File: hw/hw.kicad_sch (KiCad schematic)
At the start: 94 parts, among them U4 TPM8205ATS6

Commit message: wip
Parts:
- gave numbers to parts that had none: 89
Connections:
- net PWM1: now also U1.31 (GPIO20); no longer U1.8 (GPIO6)
- net PWM2: now also U1.32 (GPIO21); no longer U1.9 (GPIO7)
- net PWM3: now also U1.27 (GPIO16); no longer U1.11 (GPIO8)
- net PWM4: now also U1.29 (GPIO18); no longer U1.12 (GPIO9)
- net PWM5: now also U1.15 (GPIO12); no longer U1.13 (GPIO10)
- net PWM6: now also U1.17 (GPIO14); no longer U1.14 (GPIO11)
- net PWM7: now also U1.11 (GPIO8); no longer U1.15 (GPIO12)
- net PWM8: now also U1.13 (GPIO10); no longer U1.16 (GPIO13)
- net PWM9: now also U1.8 (GPIO6); no longer U1.17 (GPIO14)
- net tach1: now also U1.28 (GPIO17); no longer U1.18 (GPIO15)
- net tach2: now also U1.30 (GPIO19); no longer U1.27 (GPIO16)
- net tach3: now also U1.16 (GPIO13); no longer U1.28 (GPIO17)
- net tach4: now also U1.18 (GPIO15); no longer U1.29 (GPIO18)
- net tach5: now also U1.12 (GPIO9); no longer U1.30 (GPIO19)
- net tach6: now also U1.14 (GPIO11); no longer U1.31 (GPIO20)
- net tach7: now also U1.9 (GPIO7); no longer U1.32 (GPIO21)

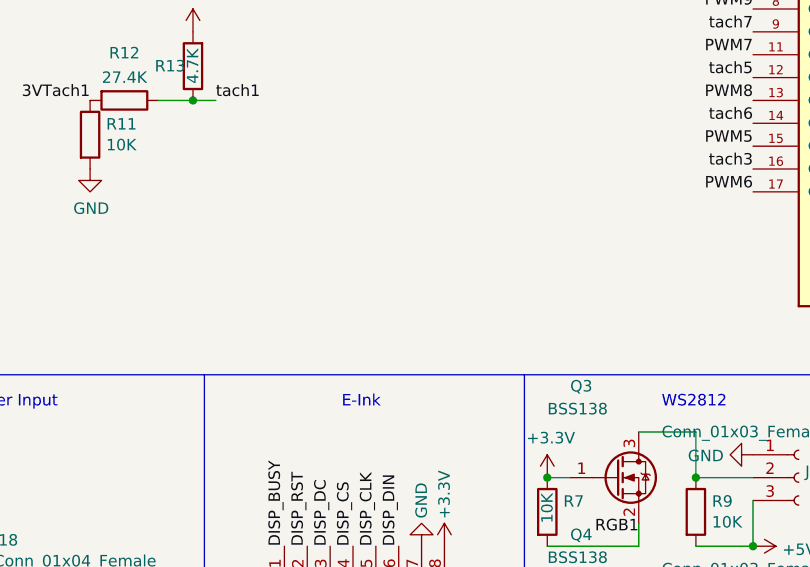
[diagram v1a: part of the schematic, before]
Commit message: add label, fix 12 v track width, connect everything
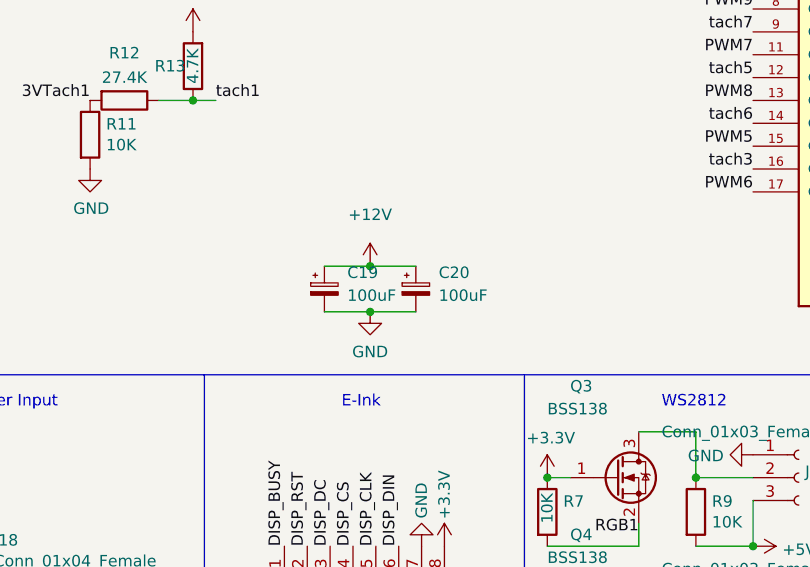
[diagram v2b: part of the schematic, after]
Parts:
- added C19, C20: 100uF, Capacitor_Tantalum_SMD:CP_EIA-7343-43_Kemet-X, symbol Device:C_Polarized_Small
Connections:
- net +12V: now also C19.1, C20.1
- net GND: now also C19.2, C20.2
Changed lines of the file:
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@@
   (junction (at 26.67 189.23) (diameter 0) (color 0 0 0 0)
   )
+  (junction (at 122.555 120.015) (diameter 0) (color 0 0 0 0)
+  )
   (junction (at 26.67 179.07) (diameter 0) (color 0 0 0 0)
   )
@@
   (junction (at 165.1 146.05) (diameter 0) (color 0 0 0 0)
   )
+  (junction (at 122.555 114.935) (diameter 0) (color 0 0 0 0)
+  )
   (junction (at 256.54 58.42) (diameter 0) (color 0 0 0 0)
   )
@@
     (stroke (width 0) (type default) (color 0 0 0 0))
   )
+  (wire (pts (xy 117.475 120.015) (xy 122.555 120.015))
+    (stroke (width 0) (type default) (color 0 0 0 0))
+  )
   (wire (pts (xy 210.82 111.76) (xy 210.82 114.3))
     (stroke (width 0) (type default) (color 0 0 0 0))
@@
     (stroke (width 0) (type default) (color 0 0 0 0))
   )
+  (wire (pts (xy 117.475 114.935) (xy 122.555 114.935))
+    (stroke (width 0) (type default) (color 0 0 0 0))
+  )
   (wire (pts (xy 73.66 45.72) (xy 69.85 45.72))
     (stroke (width 0) (type default) (color 0 0 0 0))
@@
     (stroke (width 0) (type default) (color 0 0 0 0))
   )
+  (wire (pts (xy 122.555 114.935) (xy 127.635 114.935))
+    (stroke (width 0) (type default) (color 0 0 0 0))
+  )
   (wire (pts (xy 267.97 50.8) (xy 256.54 50.8))
     (stroke (width 0) (type default) (color 0 0 0 0))
@@
     (stroke (width 0) (type default) (color 0 0 0 0))
   )
+  (wire (pts (xy 122.555 120.015) (xy 127.635 120.015))
+    (stroke (width 0) (type default) (color 0 0 0 0))
+  )
   (wire (pts (xy 256.54 58.42) (xy 267.97 58.42))
     (stroke (width 0) (type default) (color 0 0 0 0))
@@
     (pin "1")
   )
+  (symbol (lib_id "power:GND") (at 122.555 120.015 0) (unit 1)
+    (in_bom yes) (on_board yes) (fields_autoplaced)
+    (property "Reference" "#PWR0188" (id 0) (at 122.555 126.365 0)
+      (effects (font (size 1.27 1.27)) hide)
+    )
+    (property "Value" "GND" (id 1) (at 122.555 124.46 0))
+    (property "Footprint" "" (id 2) (at 122.555 120.015 0)
+      (effects (font (size 1.27 1.27)) hide)
+    )
+    (property "Datasheet" "" (id 3) (at 122.555 120.015 0)
+      (effects (font (size 1.27 1.27)) hide)
+    )
+    (pin "1")
+  )
   (symbol (lib_id "Device:D") (at 50.165 159.385 0) (unit 1)
     (in_bom yes) (on_board yes)
@@
     (pin "1")
   )
+  (symbol (lib_id "power:+12V") (at 122.555 114.935 0) (unit 1)
+    (in_bom yes) (on_board yes) (fields_autoplaced)
+    (property "Reference" "#PWR0189" (id 0) (at 122.555 118.745 0)
+      (effects (font (size 1.27 1.27)) hide)
+    )
+    (property "Value" "+12V" (id 1) (at 122.555 109.22 0))
+    (property "Footprint" "" (id 2) (at 122.555 114.935 0)
+      (effects (font (size 1.27 1.27)) hide)
+    )
+    (property "Datasheet" "" (id 3) (at 122.555 114.935 0)
+      (effects (font (size 1.27 1.27)) hide)
+    )
+    (pin "1")
+  )
   (symbol (lib_id "Device:R") (at 18.415 142.875 0) (unit 1)
     (in_bom yes) (on_board yes)
@@
     (pin "2")
   )
+  (symbol (lib_id "Device:C_Polarized_Small") (at 117.475 117.475 0) (unit 1)
+    (in_bom yes) (on_board yes) (fields_autoplaced)
+    (property "Reference" "C19" (id 0) (at 120.015 115.6588 0)
+      (effects (font (size 1.27 1.27)) (justify left))
+    )
+    (property "Value" "100uF" (id 1) (at 120.015 118.1988 0)
+      (effects (font (size 1.27 1.27)) (justify left))
+    )
+    (property "Footprint" "Capacitor_Tantalum_SMD:CP_EIA-7343-43_Kemet-X" (id 2) (at 117.475 117.475 0)
+      (effects (font (size 1.27 1.27)) hide)
+    )
+    (property "Datasheet" "~" (id 3) (at 117.475 117.475 0)
+      (effects (font (size 1.27 1.27)) hide)
+    )
+    (pin "1")
+    (pin "2")
+  )
   (symbol (lib_id "Device:R") (at 37.465 142.875 0) (unit 1)
     (in_bom yes) (on_board yes)
@@
     (pin "2")
   )
+  (symbol (lib_id "Device:C_Polarized_Small") (at 127.635 117.475 0) (unit 1)
+    (in_bom yes) (on_board yes)
+    (property "Reference" "C20" (id 0) (at 130.175 115.6588 0)
+      (effects (font (size 1.27 1.27)) (justify left))
+    )
+    (property "Value" "100uF" (id 1) (at 130.175 118.1988 0)
+      (effects (font (size 1.27 1.27)) (justify left))
+    )
+    (property "Footprint" "Capacitor_Tantalum_SMD:CP_EIA-7343-43_Kemet-X" (id 2) (at 127.635 117.475 0)
+      (effects (font (size 1.27 1.27)) hide)
+    )
+    (property "Datasheet" "~" (id 3) (at 127.635 117.475 0)
+      (effects (font (size 1.27 1.27)) hide)
+    )
+    (pin "1")
+    (pin "2")
+  )
   (symbol (lib_id "lib:TPM8205ATS6") (at 9.525 136.525 0) (unit 1)
     (in_bom yes) (on_board yes) (fields_autoplaced)
@@
       (reference "#PWR0187") (unit 1) (value "+12V") (footprint "")
     )
+    (path "/43db18ef-16bb-49c5-af0a-d68912ce76bf"
+      (reference "#PWR0188") (unit 1) (value "GND") (footprint "")
+    )
+    (path "/69a5f2b0-aa64-4372-af64-40ec78fd2320"
+      (reference "#PWR0189") (unit 1) (value "+12V") (footprint "")
+    )
     (path "/00000000-0000-0000-0000-00006338e828"
       (reference "C1") (unit 1) (value "100nF") (footprint "Capacitor_SMD:C_0402_1005Metric")
@@
       (reference "C16") (unit 1) (value "2.2uF") (footprint "Capacitor_SMD:C_0402_1005Metric")
     )
+    (path "/85e45079-cdd5-4bdf-9482-7c0eaa46ca23"
+      (reference "C19") (unit 1) (value "100uF") (footprint "Capacitor_Tantalum_SMD:CP_EIA-7343-43_Kemet-X")
+    )
+    (path "/ad236722-78c7-490e-a722-c504b46b05d9"
+      (reference "C20") (unit 1) (value "100uF") (footprint "Capacitor_Tantalum_SMD:CP_EIA-7343-43_Kemet-X")
+    )
     (path "/fccdd11b-b1f6-4078-860a-ed689ba0f747"

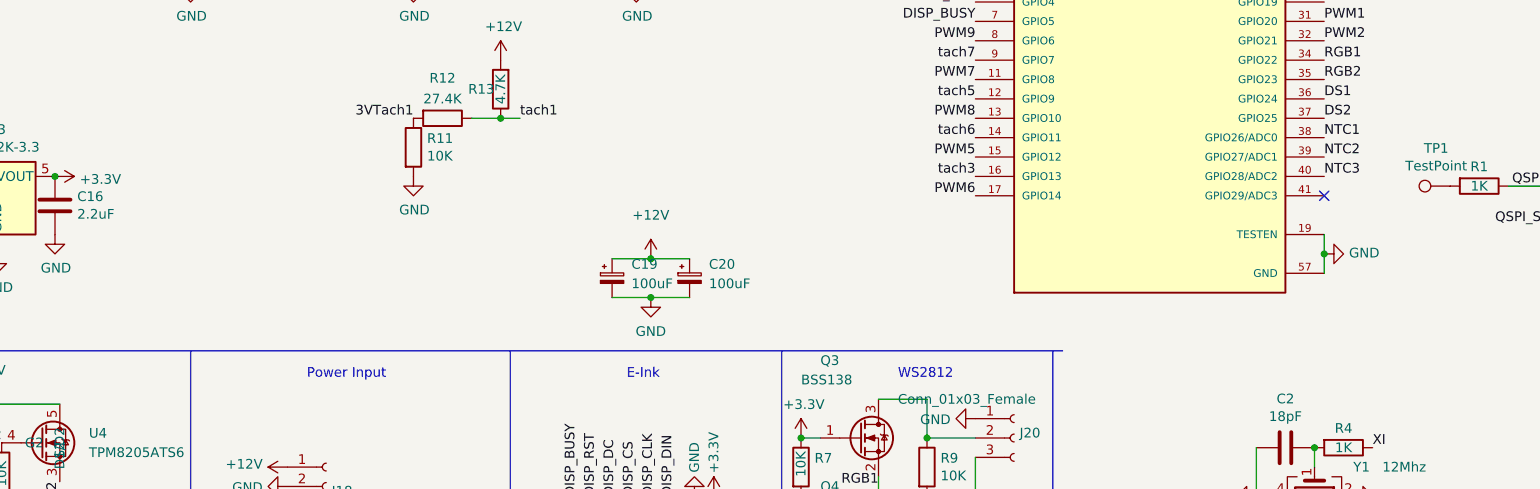
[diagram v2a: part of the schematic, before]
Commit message: add dht11/22 support
hwmon have humidity support and... i have some dht laying aroung ...
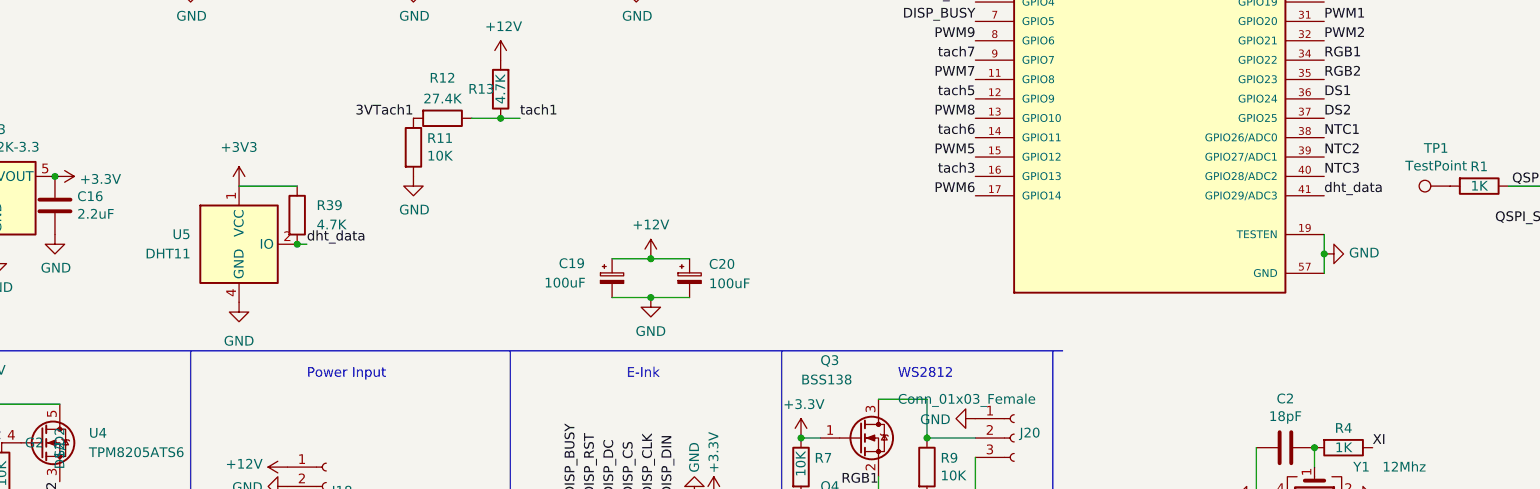
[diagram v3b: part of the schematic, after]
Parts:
- added R39: 4.7K, Resistor_SMD:R_0402_1005Metric, symbol Device:R
- added U5: DHT11, Sensor:Aosong_DHT11_5.5x12.0_P2.54mm, symbol Sensor:DHT11
- C19, C20: LCSC (none) -> C7230
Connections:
- net +3V3: now also R39.1, U5.1 (VCC)
- net GND: now also U5.4 (GND)
- net dht_data: now reaches U1.41 (GPIO29/ADC3)
- net dht_data: now also R39.2, U5.2 (IO)
- no-connect marks 11 -> 10
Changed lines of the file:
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@@
   (junction (at 165.1 162.56) (diameter 0) (color 0 0 0 0)
   )
+  (junction (at 76.2 113.03) (diameter 0) (color 0 0 0 0)
+  )
   (junction (at 210.82 33.02) (diameter 0) (color 0 0 0 0)
   )
@@
   )
   (no_connect (at 39.37 71.12))
-  (no_connect (at 210.82 106.68))
   (no_connect (at 39.37 63.5))
   (no_connect (at 39.37 68.58))
@@
     (stroke (width 0) (type default) (color 0 0 0 0))
   )
+  (wire (pts (xy 76.2 113.03) (xy 77.47 113.03))
+    (stroke (width 0) (type default) (color 0 0 0 0))
+  )
   (wire (pts (xy 201.93 139.7) (xy 201.93 146.05))
     (stroke (width 0) (type default) (color 0 0 0 0))
@@
     (stroke (width 0) (type default) (color 0 0 0 0))
   )
+  (wire (pts (xy 68.58 105.41) (xy 76.2 105.41))
+    (stroke (width 0) (type default) (color 0 0 0 0))
+  )
   (wire (pts (xy 39.37 33.02) (xy 39.37 34.29))
     (stroke (width 0) (type default) (color 0 0 0 0))
@@
     (effects (font (size 1.27 1.27)) (justify left bottom))
   )
+  (label "dht_data" (at 77.47 113.03 0)
+    (effects (font (size 1.27 1.27)) (justify left bottom))
+  )
   (label "3VTach1" (at 91.44 96.52 180)
     (effects (font (size 1.27 1.27)) (justify right bottom))
@@
     (effects (font (size 1.27 1.27)) (justify left bottom))
   )
+  (label "dht_data" (at 210.82 106.68 0)
+    (effects (font (size 1.27 1.27)) (justify left bottom))
+  )
   (label "XO" (at 165.1 63.5 180)
     (effects (font (size 1.27 1.27)) (justify right bottom))
@@
     (pin "1")
   )
+  (symbol (lib_id "power:GND") (at 68.58 120.65 0) (unit 1)
+    (in_bom yes) (on_board yes) (fields_autoplaced)
+    (property "Reference" "#PWR0190" (id 0) (at 68.58 127 0)
+      (effects (font (size 1.27 1.27)) hide)
+    )
+    (property "Value" "GND" (id 1) (at 68.58 125.73 0))
+    (property "Footprint" "" (id 2) (at 68.58 120.65 0)
+      (effects (font (size 1.27 1.27)) hide)
+    )
+    (property "Datasheet" "" (id 3) (at 68.58 120.65 0)
+      (effects (font (size 1.27 1.27)) hide)
+    )
+    (pin "1")
+  )
+  (symbol (lib_id "Sensor:DHT11") (at 68.58 113.03 0) (unit 1)
+    (in_bom yes) (on_board yes) (fields_autoplaced)
+    (property "Reference" "U5" (id 0) (at 62.23 111.7599 0)
+      (effects (font (size 1.27 1.27)) (justify right))
+    )
+    (property "Value" "DHT11" (id 1) (at 62.23 114.2999 0)
+      (effects (font (size 1.27 1.27)) (justify right))
+    )
+    (property "Footprint" "Sensor:Aosong_DHT11_5.5x12.0_P2.54mm" (id 2) (at 68.58 123.19 0)
+      (effects (font (size 1.27 1.27)) hide)
+    )
+    (property "Datasheet" "http://akizukidenshi.com/download/ds/aosong/DHT11.pdf" (id 3) (at 72.39 106.68 0)
+      (effects (font (size 1.27 1.27)) hide)
+    )
+    (pin "1")
+    (pin "2")
+    (pin "3")
+    (pin "4")
+  )
   (symbol (lib_id "power:GND") (at 122.555 120.015 0) (unit 1)
     (in_bom yes) (on_board yes) (fields_autoplaced)
@@
     (pin "2")
   )
+  (symbol (lib_id "Device:R") (at 76.2 109.22 0) (unit 1)
+    (in_bom yes) (on_board yes) (fields_autoplaced)
+    (property "Reference" "R39" (id 0) (at 78.74 107.9499 0)
+      (effects (font (size 1.27 1.27)) (justify left))
+    )
+    (property "Value" "4.7K" (id 1) (at 78.74 110.4899 0)
+      (effects (font (size 1.27 1.27)) (justify left))
+    )
+    (property "Footprint" "Resistor_SMD:R_0402_1005Metric" (id 2) (at 74.422 109.22 90)
+      (effects (font (size 1.27 1.27)) hide)
+    )
+    (property "Datasheet" "~" (id 3) (at 76.2 109.22 0)
+      (effects (font (size 1.27 1.27)) hide)
+    )
+    (pin "1")
+    (pin "2")
+  )
   (symbol (lib_id "power:GND") (at 37.465 146.685 0) (unit 1)
     (in_bom yes) (on_board yes) (fields_autoplaced)
@@
     (pin "1")
   )
-  (symbol (lib_id "power:+12V") (at 122.555 114.935 0) (unit 1)
+  (symbol (lib_id "power:+3V3") (at 68.58 105.41 0) (unit 1)
     (in_bom yes) (on_board yes) (fields_autoplaced)
+    (property "Reference" "#PWR0191" (id 0) (at 68.58 109.22 0)
+      (effects (font (size 1.27 1.27)) hide)
+    )
+    (property "Value" "+3V3" (id 1) (at 68.58 100.33 0))
+    (property "Footprint" "" (id 2) (at 68.58 105.41 0)
+      (effects (font (size 1.27 1.27)) hide)
+    )
+    (property "Datasheet" "" (id 3) (at 68.58 105.41 0)
+      (effects (font (size 1.27 1.27)) hide)
+    )
+    (pin "1")
+  )
+  (symbol (lib_id "power:+12V") (at 122.555 114.935 0) (unit 1)
+    (in_bom yes) (on_board yes)
     (property "Reference" "#PWR0189" (id 0) (at 122.555 118.745 0)
       (effects (font (size 1.27 1.27)) hide)
     )
-    (property "Value" "+12V" (id 1) (at 122.555 109.22 0))
+    (property "Value" "+12V" (id 1) (at 122.555 110.49 0))
     (property "Footprint" "" (id 2) (at 122.555 114.935 0)
       (effects (font (size 1.27 1.27)) hide)
@@
   )
   (symbol (lib_id "Device:C_Polarized_Small") (at 117.475 117.475 0) (unit 1)
-    (in_bom yes) (on_board yes) (fields_autoplaced)
-    (property "Reference" "C19" (id 0) (at 120.015 115.6588 0)
+    (in_bom yes) (on_board yes)
+    (property "Reference" "C19" (id 0) (at 110.49 115.57 0)
       (effects (font (size 1.27 1.27)) (justify left))
     )
-    (property "Value" "100uF" (id 1) (at 120.015 118.1988 0)
+    (property "Value" "100uF" (id 1) (at 108.585 118.11 0)
       (effects (font (size 1.27 1.27)) (justify left))
     )
@@
       (effects (font (size 1.27 1.27)) hide)
     )
+    (property "LCSC" "C7230" (id 4) (at 117.475 117.475 0)
+      (effects (font (size 1.27 1.27)) hide)
+    )
     (pin "1")
     (pin "2")
@@
       (effects (font (size 1.27 1.27)) hide)
     )
+    (property "LCSC" "C7230" (id 4) (at 127.635 117.475 0)
+      (effects (font (size 1.27 1.27)) hide)
+    )
     (pin "1")
     (pin "2")
@@
       (reference "#PWR0189") (unit 1) (value "+12V") (footprint "")
     )
+    (path "/1c573574-10b6-41b5-ae55-4a85969c6889"
+      (reference "#PWR0190") (unit 1) (value "GND") (footprint "")
+    )
+    (path "/66c3346e-a484-4d11-87a7-59a768ce549a"
+      (reference "#PWR0191") (unit 1) (value "+3V3") (footprint "")
+    )
     (path "/00000000-0000-0000-0000-00006338e828"
       (reference "C1") (unit 1) (value "100nF") (footprint "Capacitor_SMD:C_0402_1005Metric")
@@
       (reference "R38") (unit 1) (value "10K") (footprint "Resistor_SMD:R_0402_1005Metric")
     )
+    (path "/4dccb874-407f-41de-aea7-ecd20eb8c599"
+      (reference "R39") (unit 1) (value "4.7K") (footprint "Resistor_SMD:R_0402_1005Metric")
+    )
     (path "/00000000-0000-0000-0000-00006338dd7b"
       (reference "TP1") (unit 1) (value "TestPoint") (footprint "TestPoint:TestPoint_Pad_D1.5mm")
@@
       (reference "U4") (unit 1) (value "TPM8205ATS6") (footprint "Package_TO_SOT_SMD:TSOT-23-6")
     )
+    (path "/38f6964d-c259-4242-95b5-b9af9bf14d6c"
+      (reference "U5") (unit 1) (value "DHT11") (footprint "Sensor:Aosong_DHT11_5.5x12.0_P2.54mm")
+    )
     (path "/00000000-0000-0000-0000-000063376098"
